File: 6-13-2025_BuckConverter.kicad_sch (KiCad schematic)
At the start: 17 parts, among them J1 6V to 35V, J2 5V 3A, U1 MP2338GTL-Z

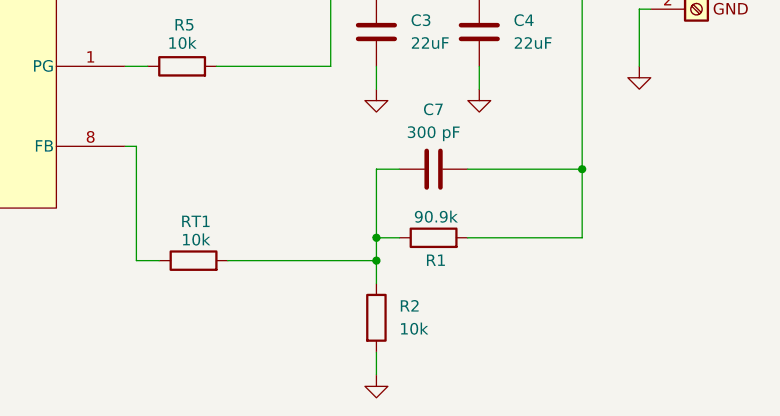
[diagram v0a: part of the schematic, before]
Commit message: Finalized layout and generated manufacturing files.
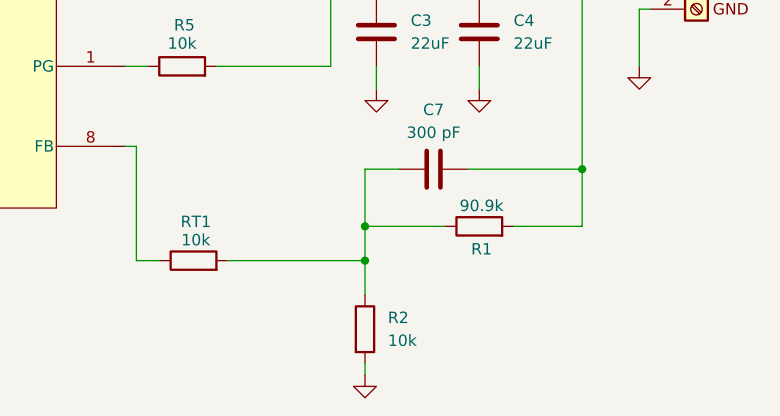
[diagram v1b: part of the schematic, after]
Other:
- moved on the sheet: R1, R2
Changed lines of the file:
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@@
 		(title "DC to DC Switching Converter")
 		(company "Teddy Kim")
-		(comment 1 "Trimming pot in para with R1")
-		(comment 2 "Change FB R's to 0.1% Tol")
-		(comment 3 "Calc curr of pins to sch")
-		(comment 4 "Calc Schematic")
-		(comment 5 "Sim schematic")
-		(comment 6 "trim pot with R1")
 	)
 	(junction
@@
 	)
 	(junction
-		(at 168.91 68.58)
+		(at 120.65 36.83)
 		(diameter 0)
 		(color 0 0 0 0)
 	)
 	(junction
-		(at 120.65 36.83)
+		(at 144.78 74.93)
 		(diameter 0)
 		(color 0 0 0 0)
@@
 	)
 	(junction
-		(at 146.05 78.74)
-		(diameter 0)
-		(color 0 0 0 0)
-	)
-	(junction
 		(at 140.97 48.26)
 		(diameter 0)
@@
 	)
 	(junction
+		(at 168.91 68.58)
+		(diameter 0)
+		(color 0 0 0 0)
+	)
+	(junction
 		(at 63.5 74.93)
 		(diameter 0)
@@
 	)
 	(junction
-		(at 146.05 76.2)
+		(at 121.92 48.26)
 		(diameter 0)
 		(color 0 0 0 0)
 	)
 	(junction
-		(at 121.92 48.26)
+		(at 144.78 78.74)
 		(diameter 0)
 		(color 0 0 0 0)
@@
 	(wire
 		(pts
+			(xy 144.78 74.93) (xy 144.78 78.74)
+		)
+		(stroke
+			(width 0)
+			(type default)
+		)
+	)
+	(wire
+		(pts
 			(xy 118.11 57.15) (xy 120.65 57.15)
 		)
@@
 	(wire
 		(pts
-			(xy 168.91 68.58) (xy 168.91 76.2)
-		)
-		(stroke
-			(width 0)
-			(type default)
-		)
-	)
-	(wire
-		(pts
 			(xy 120.65 36.83) (xy 121.92 36.83)
 		)
@@
 	(wire
 		(pts
-			(xy 156.21 76.2) (xy 168.91 76.2)
-		)
-		(stroke
-			(width 0)
-			(type default)
-		)
-	)
-	(wire
-		(pts
-			(xy 146.05 88.9) (xy 146.05 91.44)
+			(xy 144.78 90.17) (xy 144.78 91.44)
 		)
 		(stroke
@@
 	(wire
 		(pts
-			(xy 146.05 76.2) (xy 148.59 76.2)
+			(xy 168.91 68.58) (xy 168.91 74.93)
 		)
 		(stroke
@@
 	(wire
 		(pts
+			(xy 144.78 68.58) (xy 144.78 74.93)
+		)
+		(stroke
+			(width 0)
+			(type default)
+		)
+	)
+	(wire
+		(pts
 			(xy 168.91 48.26) (xy 176.53 48.26)
 		)
@@
 	(wire
 		(pts
+			(xy 144.78 78.74) (xy 144.78 82.55)
+		)
+		(stroke
+			(width 0)
+			(type default)
+		)
+	)
+	(wire
+		(pts
 			(xy 175.26 50.8) (xy 175.26 57.15)
 		)
@@
 	(wire
 		(pts
+			(xy 144.78 74.93) (xy 153.67 74.93)
+		)
+		(stroke
+			(width 0)
+			(type default)
+		)
+	)
+	(wire
+		(pts
 			(xy 55.88 36.83) (xy 67.31 36.83)
 		)
@@
 	(wire
 		(pts
+			(xy 156.21 68.58) (xy 168.91 68.58)
+		)
+		(stroke
+			(width 0)
+			(type default)
+		)
+	)
+	(wire
+		(pts
 			(xy 67.31 36.83) (xy 77.47 36.83)
 		)
@@
 	(wire
 		(pts
-			(xy 146.05 68.58) (xy 146.05 76.2)
-		)
-		(stroke
-			(width 0)
-			(type default)
-		)
-	)
-	(wire
-		(pts
-			(xy 146.05 78.74) (xy 146.05 81.28)
-		)
-		(stroke
-			(width 0)
-			(type default)
-		)
-	)
-	(wire
-		(pts
 			(xy 50.8 52.07) (xy 50.8 46.99)
 		)
@@
 	(wire
 		(pts
-			(xy 148.59 68.58) (xy 146.05 68.58)
+			(xy 148.59 68.58) (xy 144.78 68.58)
 		)
 		(stroke
@@
 	(wire
 		(pts
-			(xy 146.05 76.2) (xy 146.05 78.74)
-		)
-		(stroke
-			(width 0)
-			(type default)
-		)
-	)
-	(wire
-		(pts
-			(xy 156.21 68.58) (xy 168.91 68.58)
-		)
-		(stroke
-			(width 0)
-			(type default)
-		)
-	)
-	(wire
-		(pts
 			(xy 63.5 62.23) (xy 77.47 62.23)
 		)
@@
 	(wire
 		(pts
+			(xy 161.29 74.93) (xy 168.91 74.93)
+		)
+		(stroke
+			(width 0)
+			(type default)
+		)
+	)
+	(wire
+		(pts
 			(xy 121.92 45.72) (xy 121.92 48.26)
 		)
@@
 	(wire
 		(pts
-			(xy 129.54 78.74) (xy 146.05 78.74)
+			(xy 129.54 78.74) (xy 144.78 78.74)
 		)
 		(stroke
@@
 	(symbol
 		(lib_id "Device:R")
-		(at 146.05 85.09 0)
+		(at 144.78 86.36 0)
 		(unit 1)
 		(exclude_from_sim no)
@@
 		(dnp no)
 		(property "Reference" "R2"
-			(at 148.59 83.8199 0)
+			(at 147.32 85.0899 0)
 			(effects
 				(font
@@
 		)
 		(property "Value" "10k"
-			(at 148.59 86.3599 0)
+			(at 147.32 87.6299 0)
 			(effects
 				(font
@@
 		)
 		(property "Footprint" "Resistor_SMD:R_0805_2012Metric_Pad1.20x1.40mm_HandSolder"
-			(at 144.272 85.09 90)
+			(at 143.002 86.36 90)
 			(effects
 				(font
@@
 		)
 		(property "Datasheet" "~"
-			(at 146.05 85.09 0)
+			(at 144.78 86.36 0)
 			(effects
 				(font
@@
 		)
 		(property "Description" "Resistor"
-			(at 146.05 85.09 0)
+			(at 144.78 86.36 0)
 			(effects
 				(font
@@
 		)
 		(property "ID" "P10KDACT-ND"
-			(at 146.05 85.09 0)
+			(at 144.78 86.36 0)
 			(effects
 				(font
@@
 	(symbol
 		(lib_id "power:GND")
-		(at 146.05 91.44 0)
+		(at 144.78 91.44 0)
 		(unit 1)
 		(exclude_from_sim no)
@@
 		(fields_autoplaced yes)
 		(property "Reference" "#PWR07"
-			(at 146.05 97.79 0)
+			(at 144.78 97.79 0)
 			(effects
 				(font
@@
 		)
 		(property "Value" "GND"
-			(at 146.05 96.52 0)
+			(at 144.78 96.52 0)
 			(effects
 				(font
@@
 		)
 		(property "Footprint" ""
-			(at 146.05 91.44 0)
+			(at 144.78 91.44 0)
 			(effects
 				(font
@@
 		)
 		(property "Datasheet" ""
-			(at 146.05 91.44 0)
+			(at 144.78 91.44 0)
 			(effects
 				(font
@@
 		)
 		(property "Description" "Power symbol creates a global label with name \"GND\" , ground"
-			(at 146.05 91.44 0)
+			(at 144.78 91.44 0)
 			(effects
 				(font
@@
 	(symbol
 		(lib_id "Device:R")
-		(at 152.4 76.2 90)
+		(at 157.48 74.93 90)
 		(unit 1)
 		(exclude_from_sim no)
@@
 		(dnp no)
 		(property "Reference" "R1"
-			(at 152.654 78.74 90)
+			(at 157.734 77.47 90)
 			(effects
 				(font
@@
 		)
 		(property "Value" "90.9k"
-			(at 152.654 73.914 90)
+			(at 157.734 72.644 90)
 			(effects
 				(font
@@
 		)
 		(property "Footprint" "Resistor_SMD:R_0805_2012Metric_Pad1.20x1.40mm_HandSolder"
-			(at 152.4 77.978 90)
+			(at 157.48 76.708 90)
 			(effects
 				(font
@@
 		)
 		(property "Datasheet" "~"
-			(at 152.4 76.2 0)
+			(at 157.48 74.93 0)
 			(effects
 				(font
@@
 		)
 		(property "Description" "Resistor"
-			(at 152.4 76.2 0)
+			(at 157.48 74.93 0)
 			(effects
 				(font
@@
 		)
 		(property "ID" "P90.9KDACT-ND"
-			(at 152.4 76.2 90)
-			(effects
-				(font
+			(at 157.48 74.93 90)
+			(effects
+				(font
